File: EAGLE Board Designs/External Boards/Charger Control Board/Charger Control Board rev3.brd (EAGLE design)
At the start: 87.6 x 99.1 mm, 62 parts

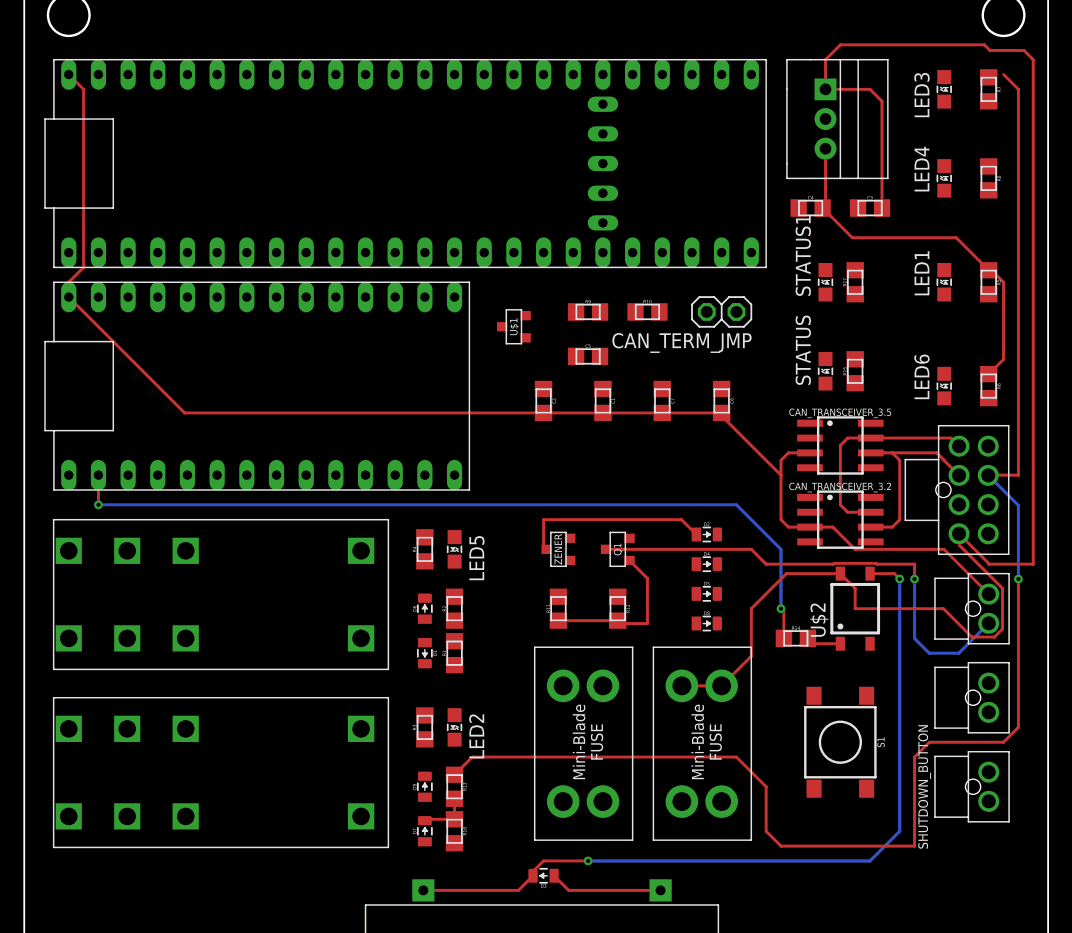
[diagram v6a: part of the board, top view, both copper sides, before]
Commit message: Trace_Width_Increase
Trace width increase in progress
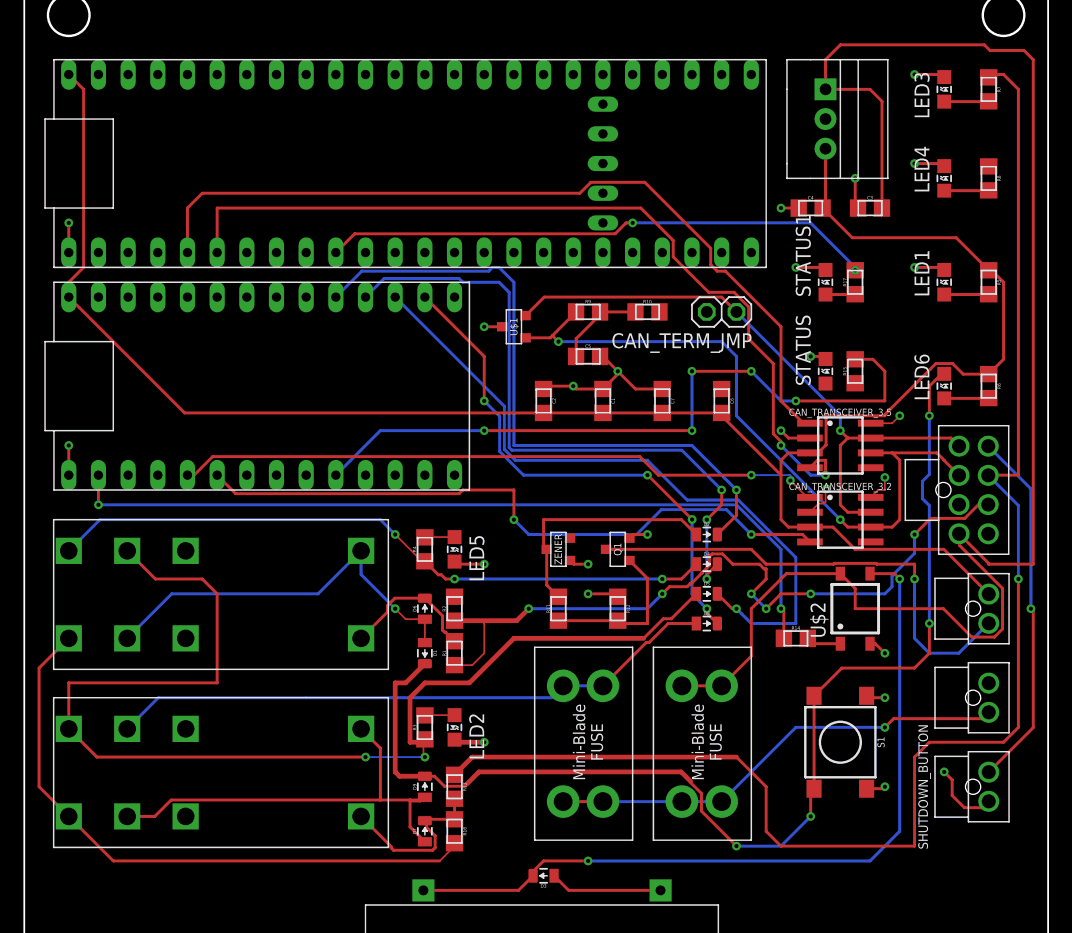
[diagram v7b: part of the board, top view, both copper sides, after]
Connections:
- new net BMS_OK_RELAY: BMS_SHUTDOWN_RLY.COIL+, D6.C, R1.2
- net BMS_OK: no longer BMS_SHUTDOWN_RLY.COIL+, D6.C, R1.2
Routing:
- net SHUTDOWN_B: track 0.00 -> 99.8 mm, vias 0 -> 2
- net LATCH_EXT_BUTTON: track 0.00 -> 99.1 mm, vias 0 -> 4
- net N$4: track 0.00 -> 74.4 mm, vias 0 -> 2
- net N$6: track 0.00 -> 71.1 mm
- net BMS_OK: track 0.00 -> 66.8 mm, vias 0 -> 6
- net SHUTDOWN_C: track 0.00 -> 63.5 mm, vias 0 -> 4
- net GND: track 9.63 -> 73.1 mm, vias 0 -> 24
- net N$11: track 0.00 -> 60.2 mm, vias 0 -> 5
- net SHUTDOWN_B_TEENSY: track 0.00 -> 59.1 mm, vias 0 -> 1
- net N$15: track 0.00 -> 56.6 mm, vias 0 -> 2
- net SHUTDOWN_C_TEENSY: track 0.00 -> 56.2 mm, vias 0 -> 3
- net SHUTDOWN_D_TEENSY: track 0.00 -> 55.9 mm, vias 0 -> 1
- net N$22: track 0.00 -> 55.8 mm, vias 0 -> 2
- net N$60: track 0.00 -> 52.7 mm
- net SHUTDOWN_A: track 0.00 -> 52.4 mm
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
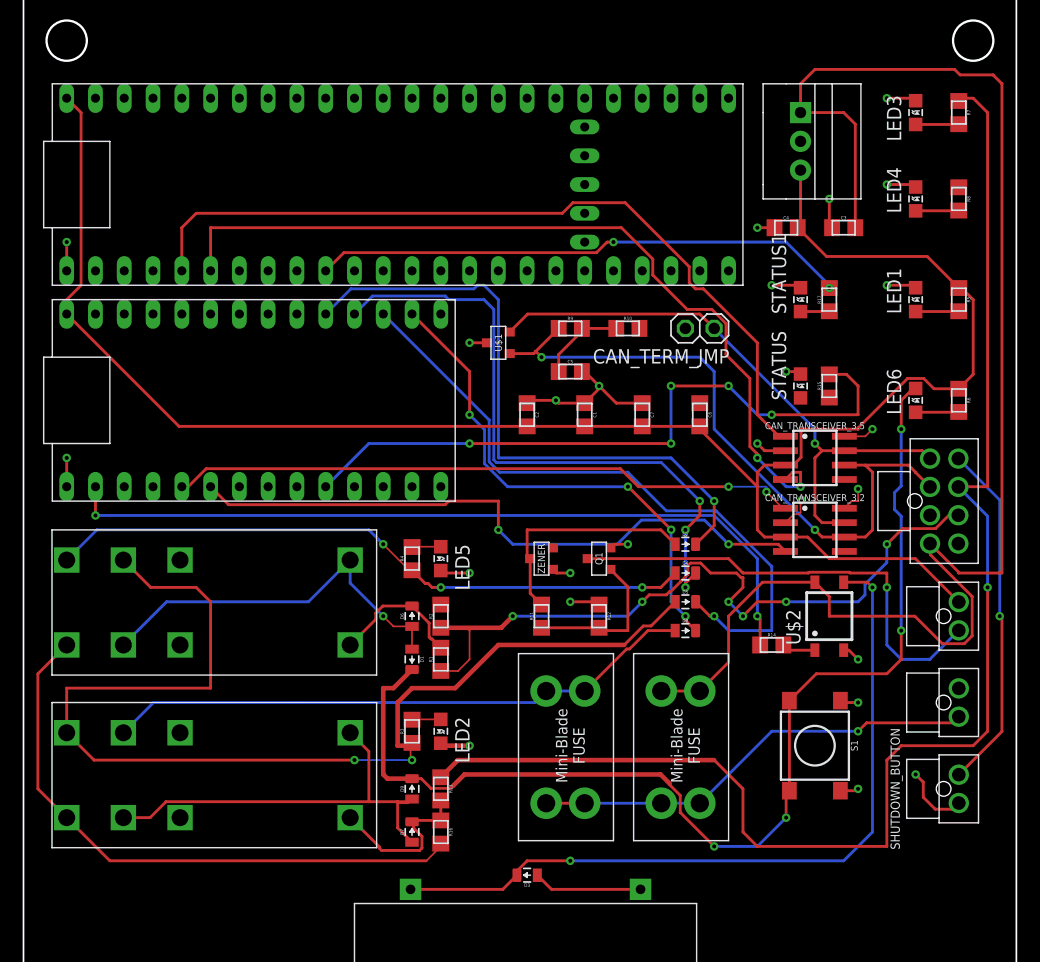
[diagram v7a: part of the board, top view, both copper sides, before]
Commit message: Update_Routing
All connections are made, pending reiew
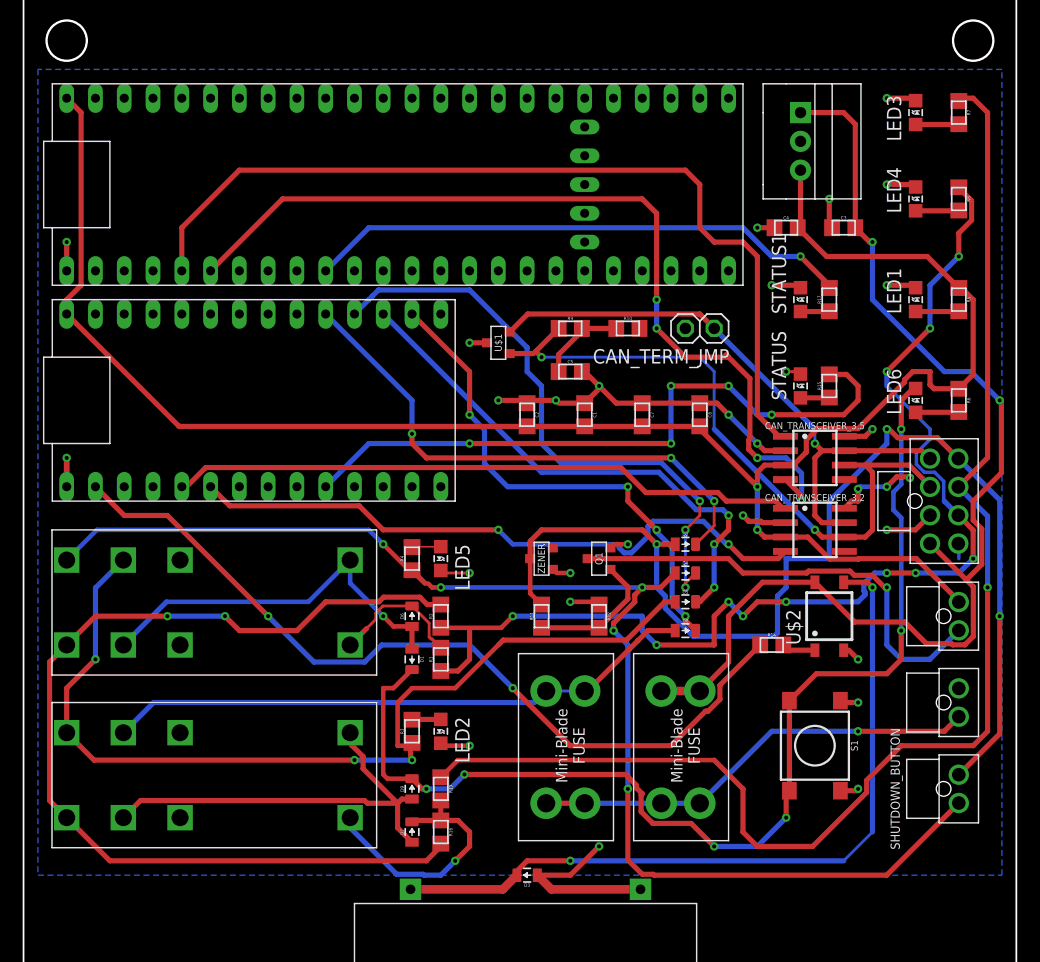
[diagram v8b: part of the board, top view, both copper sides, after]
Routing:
- net SHUTDOWN_C: track 63.5 -> 115.5 mm, vias 4 -> 5
- net SHUTDOWN_D: track 52.8 -> 100.2 mm, vias 1 -> 3
- net BMS_OK: track 66.8 -> 104.8 mm, vias 6 -> 11
- net N$60: track 52.7 -> 87.9 mm, vias 0 -> 2
- net +12V: track 133.4 -> 100.6 mm, vias 0 -> 2
- net GND: track 73.1 -> 104.7 mm, vias 24 -> 30
- net SHUTDOWN_B: track 99.8 -> 83.6 mm, vias 2 -> 3
- net SHUTDOWN_B_TEENSY: track 59.1 -> 46.9 mm, vias 1 -> 3
- net N$6: track 71.1 -> 79.3 mm
- net SHUTDOWN_D_TEENSY: track 55.9 -> 47.8 mm, vias 1 -> 3
- net N$4: track 74.4 -> 79.8 mm, vias 2 -> 4
- net TOGGLE_CHARGER: track 70.3 -> 73.8 mm
- net SHUTDOWN_C_TEENSY: track 56.2 -> 53.1 mm
- net OKHS: track 139.2 -> 141.9 mm, vias 1 -> 2
- net N$8: track 0.00 -> 2.55 mm
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- added copper zone on layer 16, net GND
